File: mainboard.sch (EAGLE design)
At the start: 6 parts, among them U1 ATMEGA2560AU, U2 ITG-3200

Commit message: Added documentation
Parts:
- added IC1: FT232RLSSOP, SparkFun:FT232RLSSOP
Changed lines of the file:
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@@
 <part name="U2" library="SparkFun-Sensors" deviceset="ITG-3200" device=""/>
 <part name="U$2" library="SparkFun-Sensors" deviceset="HMC5883L" device="SMD"/>
+<part name="IC1" library="SparkFun" deviceset="FT232RL" device="SSOP"/>
 </parts>
 <sheets>
@@
 <instance part="U2" gate="G$1" x="-66.04" y="-12.7"/>
 <instance part="U$2" gate="G$1" x="-58.42" y="-60.96"/>
+<instance part="IC1" gate="G$1" x="-99.06" y="35.56"/>
 </instances>
 <busses>

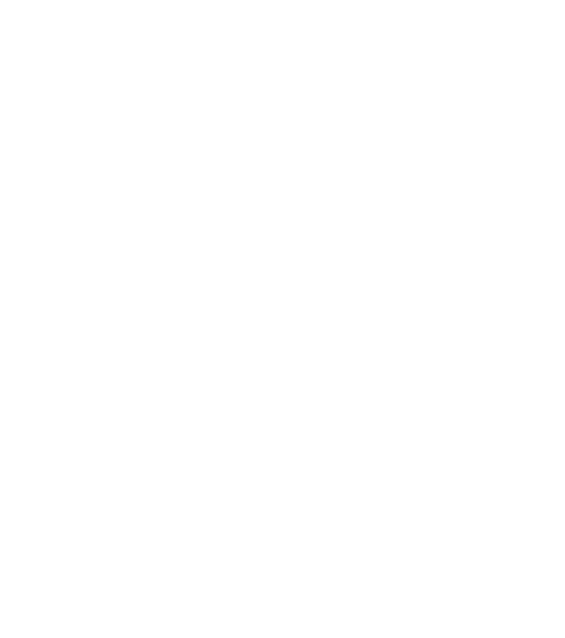
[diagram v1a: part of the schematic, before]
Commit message: Added level shifter
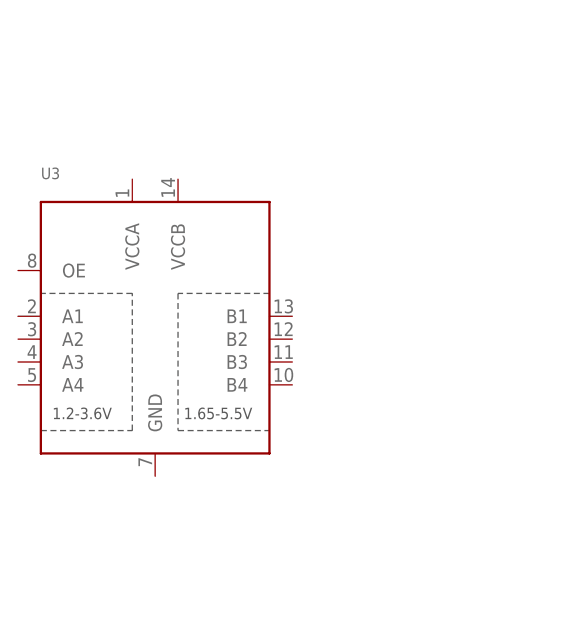
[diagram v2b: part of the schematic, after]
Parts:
- added U3: (no value), SparkFun-DigitalIC:TXB0104PWR
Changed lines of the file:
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@@
 <part name="U$2" library="SparkFun-Sensors" deviceset="HMC5883L" device="SMD"/>
 <part name="IC1" library="SparkFun" deviceset="FT232RL" device="SSOP"/>
+<part name="U3" library="SparkFun-DigitalIC" deviceset="TXB0104PWR" device=""/>
 </parts>
 <sheets>
@@
 <instance part="U$2" gate="G$1" x="-58.42" y="-60.96"/>
 <instance part="IC1" gate="G$1" x="-99.06" y="35.56"/>
+<instance part="U3" gate="G$1" x="-147.32" y="-30.48"/>
 </instances>
 <busses>

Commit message: Initial commit of power board
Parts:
- removed IC1: FT232RLSSOP, SparkFun:FT232RLSSOP
- removed U$1: RFM23BP, RFM23BP:RFM23BP
- removed U$2: HMC5883LSMD, SparkFun-Sensors:HMC5883LSMD
- added C1, C10, C2, C3, C5, C6, C7, C8, C9: 0.1uF, SparkFun:CAP0603-CAP
- added C4: 0.1uF, SparkFun:CAP0402-CAP
- added JP1, JP2: USB-SMD-NS, SparkFun-Connectors:USB-SMD-NS
- added LED2: yellow, SparkFun:LED0603
- added R1, R4, R5: 10k, SparkFun:RESISTOR0603-RES
- added R3: 10k, SparkFun:RESISTOR0402-RES
- added R7: 470, SparkFun:RESISTOR0402-RES
- added SMA1: BU-SMA-V, con-coax:BU-SMA-V
- added U4: HMC5883LSMD, SparkFun-Sensors:HMC5883LSMD
- added U5: ITG-3200, SparkFun-Sensors:ITG-3200
- added U6: (no value), SparkFun-DigitalIC:TXB0104PWR
- added U7: ATMEGA328P, SparkFun:ATMEGA168
- added U8: FT232RLSSOP, SparkFun:FT232RLSSOP
- added Y1: RESONATORSMD, SparkFun:RESONATORSMD
- added Y2: 16MHZ, SparkFun-FreqCtrl:RESONATOR16MHZ
- U1: device SparkFun-DigitalIC:ATMEGA2560AU -> SparkFun:ATMEGA2560AU
- U2: value ITG-3200 -> FT232RLSSOP; device SparkFun-Sensors:ITG-3200 -> SparkFun:FT232RLSSOP
- U3: value (none) -> RFM23BP; device SparkFun-DigitalIC:TXB0104PWR -> RFM23BP:RFM23BP
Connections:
- new net 3.3V: C6.1, C7.1, C8.1, R3.2, R4.2, R5.2, U1.AVCC, U1.VCC, U1.VCC1, U1.VCC2, U1.VCC3, U6.VCCA
- new net 5V: C2.1, C3.1, C9.1, R1.2, U3.VCC, U6.VCCB, U7.AVCC, U7.VCC@1, U7.VCC@2
- new net A0: U1.(ADC0)PF0
- new net A1: U1.(ADC1)PF1
- new net A10: U1.PK2(ADC10/PCINT18)
- new net A11: U1.PK3(ADC11/PCINT19)
- new net A12: U1.PK4(ADC12/PCINT20)
- new net A13: U1.PK5(ADC13/PCINT21)
- new net A14: U1.PK6(ADC14/PCINT22)
- new net A15: U1.PK7(ADC15/PCINT23)
- new net A2: U1.(ADC2)PF2
- new net A3: U1.(ADC3)PF3
- new net A4: U1.(ADC4/TCK)PF4
- new net A5: U1.(ADC5/TMS)PF5
- new net A6: U1.(ADC6/TDO)PF6
- new net A7: U1.(ADC7/TDI)PF7
- new net A8: U1.PK0(ADC8/PCINT16)
- new net A9: U1.PK1(ADC9/PCINT17)
- new net AREF: C5.1, U1.AREF
- new net DTR: C4.1
- new net DTR2: C1.1
- new net GND: C10.2, C2.2, C3.2, C5.2, C6.2, C7.2, C8.2, C9.2, LED2.C, SMA1.2, U1.AGND, U1.GND, U1.GND1, U1.GND2, U1.GND3, U3.GND1, U3.GND2, U3.GND3, U6.GND, U7.AGND, U7.GND@1, U7.GND@2, Y1.2, Y2.2
- new net MISO2: U3.SDO, U7.PB4(MISO)
- new net MOSI2: U3.SDI, U7.PB3(MOSI/OC2)
- new net N$1: SMA1.1, U3.ANT
- new net N$2: U7.PB6(XTAL1/TOSC1), Y2.1
- new net N$3: LED2.A, R7.1
- new net N$4: C10.1, U7.AREF
- new net N$5: U7.PB7(XTAL2/TOSC2), Y2.3
- new net N$73: U1.XTAL2, Y1.1
- new net N$74: U1.XTAL1, Y1.3
- new net PA0: U1.(AD0)PA0
- new net PA1: U1.(AD1)PA1
- new net PA2: U1.(AD2)PA2
- new net PA3: U1.(AD3)PA3
- new net PA4: U1.(AD4)PA4
- new net PA5: U1.(AD5)PA5
- new net PA6: U1.(AD6)PA6
- new net PA7: U1.(AD7)PA7
- new net PB0: U1.(SS/PCINT0)PB0
- new net PB1: U1.(SCK/PCINT1)PB1
- new net PB2: U1.(MOSI/PCINT2)PB2
- new net PB3: U1.(MISO/PCINT3)PB3
- new net PB4: U1.(OC2A/PCINT4)PB4
- new net PB5: U1.(OC1A/PCINT5)PB5
- new net PB6: U1.(OC1B/PCINT6)PB6
- new net PB7: R7.2, U1.(OC0A/OC1C/PCINT7)PB7
- new net PC0: U1.(A8)PC0
- new net PC1: U1.(A9)PC1
- new net PC2: U1.(A10)PC2
- new net PC3: U1.(A11)PC3
- new net PC4: U1.(A12)PC4
- new net PC5: U1.(A13)PC5
- new net PC6: U1.(A14)PC6
- new net PC7: U1.(A15)PC7
- new net PD7: U1.(T0)PD7
- new net PE3: U1.(OC3A/AIN1)PE3
- new net PE4: U1.(OC3B/INT4)PE4
- new net PE5: U1.(OC3C/INT5)PE5
- new net PG0: U1.(WR)PG0
- new net PG1: U1.(RD)PG1
- new net PG2: U1.(ALE)PG2
- new net PG5: U1.(OC0B)PG5
- new net PH3: U1.PH3(OC4A)
- new net PH4: U1.PH4(OC4B)
- new net PH5: U1.PH5(OC4C)
- new net PH6: U1.PH6(OC2B)
- new net PL0: U1.PL0(ICP4)
- new net PL1: U1.PL1(ICP5)
- new net PL2: U1.PL2(T5)
- new net PL3: U1.PL3(OC5A)
- new net PL4: U1.PL4(OC5B)
- new net PL5: U1.PL5(OC5C)
- new net PL6: U1.PL6
- new net PL7: U1.PL7
- new net RESET: C4.2, R3.1, U1.RESET
- new net RESET2: C1.2, R1.1, U7.PC6(/RESET)
- new net RX0: U1.(RXD0/PCIN8)PE0
- new net RX1: U1.(RXD1/INT2)PD2
- new net RX2: U1.PH0(RXD2)
- new net RX3: U1.PJ0(RXD3/PCINT9)
- new net SCK2: U3.SCK, U7.PB5(SCK)
- new net SCL: R5.1, U1.(SCL/INT0)PD0
- new net SDA: R4.1, U1.(SDA/INT1)PD1
- new net TX0: U1.(TXD0)PE1
- new net TX1: U1.(TXD1/INT3)PD3
- new net TX2: U1.PH1(TXD2)
- new net TX3: U1.PJ1(TXD3/PCINT10)
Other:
- note added: "8MHz"
- note added: "ATMEGA2560V"
- moved on the sheet: U1

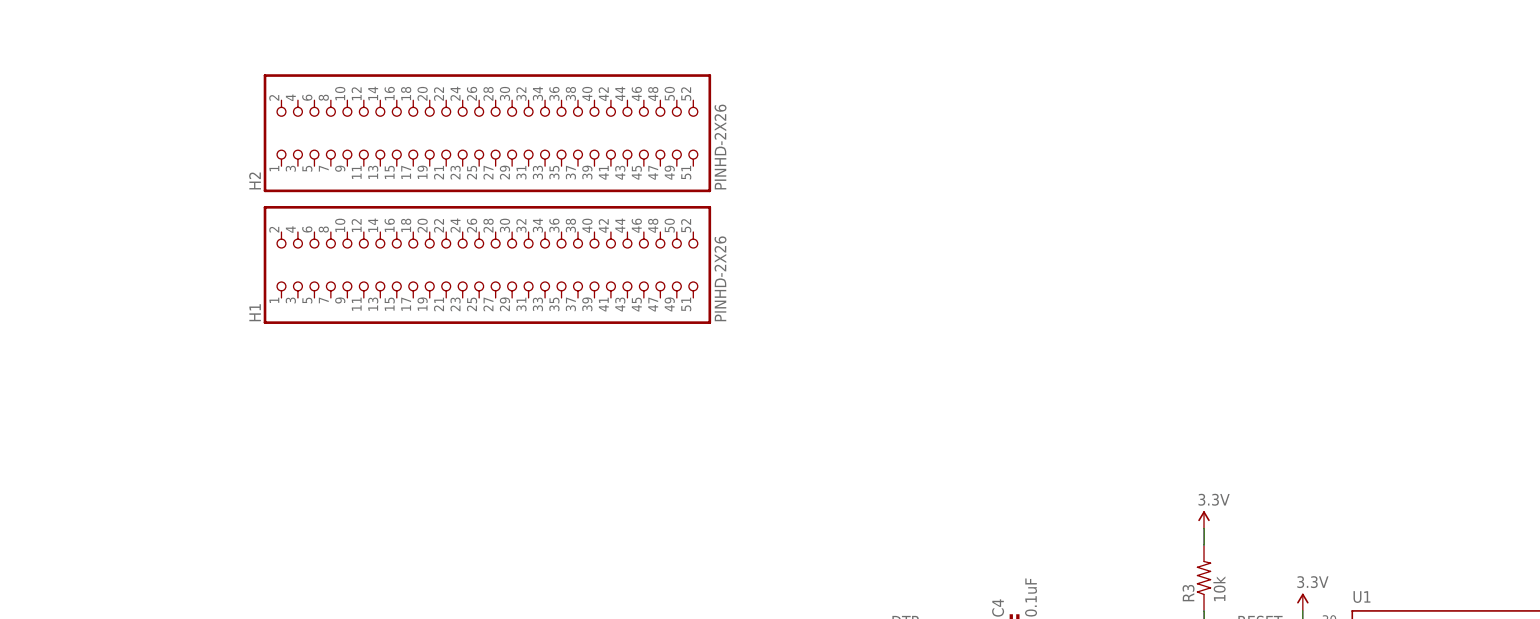
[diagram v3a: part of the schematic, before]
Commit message: Added RTC
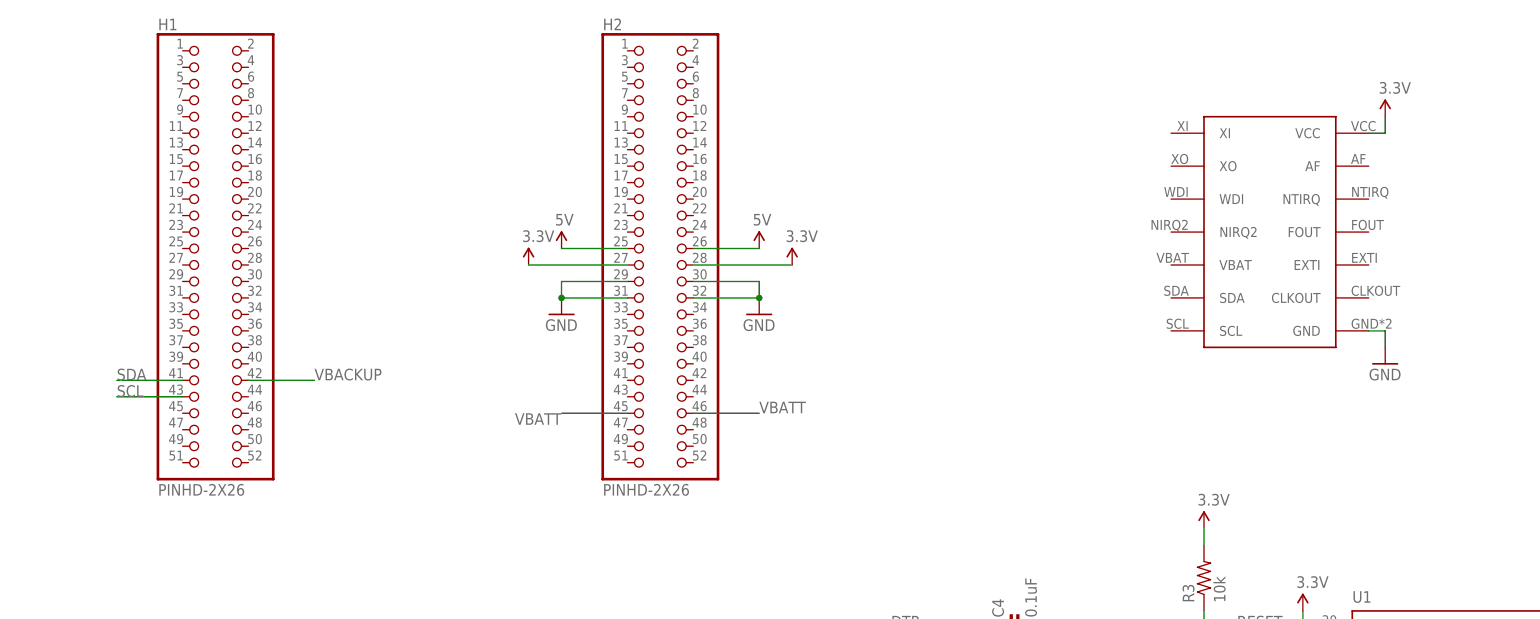
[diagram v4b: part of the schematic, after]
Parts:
- added U$1: AB0805, AB0805:AB0805
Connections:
- new net VBACKUP: H1.42
- new net VBATT: H2.45, H2.46
- net 3.3V: now also H2.27, H2.28, U$1.VCC
- net 5V: now also H2.25, H2.26
- net GND: now also H2.29, H2.30, H2.31, H2.32, U$1.GND
- net SCL: now also H1.43
- net SDA: now also H1.41
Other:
- moved on the sheet: H1, H2
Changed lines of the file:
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@@
 <part name="P+2" library="SparkFun" deviceset="3.3V" device=""/>
 <part name="GND11" library="SparkFun" deviceset="GND" device=""/>
+<part name="SUPPLY5" library="SparkFun-Aesthetics" deviceset="5V" device=""/>
+<part name="SUPPLY6" library="SparkFun-Aesthetics" deviceset="5V" device=""/>
+<part name="P+3" library="SparkFun" deviceset="3.3V" device=""/>
+<part name="P+4" library="SparkFun" deviceset="3.3V" device=""/>
+<part name="GND12" library="SparkFun" deviceset="GND" device=""/>
+<part name="GND14" library="SparkFun" deviceset="GND" device=""/>
+<part name="U$1" library="AB0805" deviceset="AB0805" device=""/>
+<part name="GND15" library="SparkFun" deviceset="GND" device=""/>
+<part name="P+7" library="SparkFun" deviceset="3.3V" device=""/>
 </parts>
 <sheets>
@@
 </plain>
 <instances>
-<instance part="H1" gate="G$1" x="50.8" y="114.3" rot="R90"/>
-<instance part="H2" gate="G$1" x="50.8" y="134.62" rot="R90"/>
+<instance part="H1" gate="G$1" x="10.16" y="116.84"/>
+<instance part="H2" gate="G$1" x="78.74" y="116.84"/>
 <instance part="U3" gate="G$1" x="-45.72" y="50.8"/>
 <instance part="U5" gate="G$1" x="347.98" y="0"/>
@@
 <instance part="P+2" gate="G$1" x="50.8" y="12.7"/>
 <instance part="GND11" gate="1" x="53.34" y="-27.94"/>
+<instance part="SUPPLY5" gate="G$1" x="63.5" y="116.84"/>
+<instance part="SUPPLY6" gate="G$1" x="93.98" y="116.84"/>
+<instance part="P+3" gate="G$1" x="58.42" y="114.3"/>
+<instance part="P+4" gate="G$1" x="99.06" y="114.3"/>
+<instance part="GND12" gate="1" x="63.5" y="106.68"/>
+<instance part="GND14" gate="1" x="93.98" y="106.68"/>
+<instance part="U$1" gate="G$1" x="172.72" y="119.38"/>
+<instance part="GND15" gate="1" x="190.5" y="99.06"/>
+<instance part="P+7" gate="G$1" x="190.5" y="137.16"/>
 </instances>
 <busses>
@@
 <wire x1="53.34" y1="-25.4" x2="53.34" y2="-22.86" width="0.1524" layer="91"/>
 </segment>
+<segment>
+<pinref part="H2" gate="G$1" pin="29"/>
+<wire x1="73.66" y1="111.76" x2="63.5" y2="111.76" width="0.1524" layer="91"/>
+<pinref part="H2" gate="G$1" pin="31"/>
+<wire x1="73.66" y1="109.22" x2="63.5" y2="109.22" width="0.1524" layer="91"/>
+<wire x1="63.5" y1="111.76" x2="63.5" y2="109.22" width="0.1524" layer="91"/>
+<pinref part="GND12" gate="1" pin="GND"/>
+<junction x="63.5" y="109.22"/>
+</segment>
+<segment>
+<pinref part="H2" gate="G$1" pin="30"/>
+<wire x1="83.82" y1="111.76" x2="93.98" y2="111.76" width="0.1524" layer="91"/>
+<pinref part="H2" gate="G$1" pin="32"/>
+<wire x1="83.82" y1="109.22" x2="93.98" y2="109.22" width="0.1524" layer="91"/>
+<wire x1="93.98" y1="111.76" x2="93.98" y2="109.22" width="0.1524" layer="91"/>
+<pinref part="GND14" gate="1" pin="GND"/>
+<junction x="93.98" y="109.22"/>
+</segment>
+<segment>
+<pinref part="U$1" gate="G$1" pin="GND"/>
+<wire x1="187.96" y1="104.14" x2="190.5" y2="104.14" width="0.1524" layer="91"/>
+<wire x1="190.5" y1="104.14" x2="190.5" y2="101.6" width="0.1524" layer="91"/>
+<pinref part="GND15" gate="1" pin="GND"/>
+</segment>
 </net>
 <net name="N$73" class="0">
@@
 <pinref part="R5" gate="G$1" pin="1"/>
 </segment>
+<segment>
+<pinref part="H1" gate="G$1" pin="43"/>
+<wire x1="5.08" y1="93.98" x2="-5.08" y2="93.98" width="0.1524" layer="91"/>
+<label x="-5.08" y="93.98" size="1.778" layer="95"/>
+</segment>
 </net>
 <net name="SDA" class="0">
@@
 <pinref part="R4" gate="G$1" pin="1"/>
 <pinref part="U1" gate="1" pin="(SDA/INT1)PD1"/>
+</segment>
+<segment>
+<pinref part="H1" gate="G$1" pin="41"/>
+<wire x1="5.08" y1="96.52" x2="-5.08" y2="96.52" width="0.1524" layer="91"/>
+<label x="-5.08" y="96.52" size="1.778" layer="95"/>
 </segment>
 </net>
@@
 <wire x1="50.8" y1="12.7" x2="50.8" y2="10.16" width="0.1524" layer="91"/>
 </segment>
+<segment>
+<pinref part="H2" gate="G$1" pin="27"/>
+<wire x1="73.66" y1="114.3" x2="58.42" y2="114.3" width="0.1524" layer="91"/>
+<pinref part="P+3" gate="G$1" pin="3.3V"/>
+</segment>
+<segment>
+<pinref part="H2" gate="G$1" pin="28"/>
+<wire x1="83.82" y1="114.3" x2="99.06" y2="114.3" width="0.1524" layer="91"/>
+<pinref part="P+4" gate="G$1" pin="3.3V"/>
+</segment>
+<segment>
+<pinref part="U$1" gate="G$1" pin="VCC"/>
+<pinref part="P+7" gate="G$1" pin="3.3V"/>
+<wire x1="187.96" y1="134.62" x2="190.5" y2="134.62" width="0.1524" layer="91"/>
+<wire x1="190.5" y1="134.62" x2="190.5" y2="137.16" width="0.1524" layer="91"/>
+</segment>
 </net>
 <net name="RESET2" class="0">
@@
 </segment>
 <segment>
+<pinref part="SUPPLY2" gate="G$1" pin="5V"/>
 <pinref part="U3" gate="G$1" pin="VCC"/>
-<pinref part="SUPPLY2" gate="G$1" pin="5V"/>
 <wire x1="-45.72" y1="66.04" x2="-45.72" y2="68.58" width="0.1524" layer="91"/>
 </segment>
@@
 <wire x1="55.88" y1="10.16" x2="55.88" y2="12.7" width="0.1524" layer="91"/>
 </segment>
+<segment>
+<pinref part="H2" gate="G$1" pin="25"/>
+<wire x1="73.66" y1="116.84" x2="63.5" y2="116.84" width="0.1524" layer="91"/>
+<pinref part="SUPPLY5" gate="G$1" pin="5V"/>
+</segment>
+<segment>
+<pinref part="H2" gate="G$1" pin="26"/>
+<wire x1="83.82" y1="116.84" x2="93.98" y2="116.84" width="0.1524" layer="91"/>
+<pinref part="SUPPLY6" gate="G$1" pin="5V"/>
+</segment>
 </net>
 <net name="N$1" class="0">
@@
 </segment>
 </net>
+<net name="VBATT" class="0">
+<segment>
+<pinref part="H2" gate="G$1" pin="45"/>
+<wire x1="73.66" y1="91.44" x2="63.5" y2="91.44" width="0.1524" layer="91"/>
+<label x="63.5" y="91.44" size="1.778" layer="95" rot="R180"/>
+</segment>
+<segment>
+<pinref part="H2" gate="G$1" pin="46"/>
+<wire x1="83.82" y1="91.44" x2="93.98" y2="91.44" width="0.1524" layer="91"/>
+<label x="93.98" y="91.44" size="1.778" layer="95"/>
+</segment>
+</net>
+<net name="VBACKUP" class="0">
+<segment>
+<pinref part="H1" gate="G$1" pin="42"/>
+<wire x1="15.24" y1="96.52" x2="25.4" y2="96.52" width="0.1524" layer="91"/>
+<label x="25.4" y="96.52" size="1.778" layer="95"/>
+</segment>
+</net>

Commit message: Added Micrel voltage supervisors
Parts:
- added U10: MIC803-46D3VM3TR, Micrel:MIC803-46D3VM3TR
- added U9: MIC803-31D3VM3TR, Micrel:MIC803-31D3VM3TR
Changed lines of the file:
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@@
 <part name="GND15" library="SparkFun" deviceset="GND" device=""/>
 <part name="P+7" library="SparkFun" deviceset="3.3V" device=""/>
+<part name="U9" library="Micrel" deviceset="MIC803-31D3VM3TR" device=""/>
+<part name="U10" library="Micrel" deviceset="MIC803-46D3VM3TR" device=""/>
 </parts>
 <sheets>
@@
 <instance part="GND13" gate="1" x="271.78" y="5.08"/>
 <instance part="P+1" gate="G$1" x="162.56" y="73.66"/>
-<instance part="P+5" gate="G$1" x="177.8" y="60.96"/>
+<instance part="P+5" gate="G$1" x="177.8" y="83.82"/>
 <instance part="P+6" gate="G$1" x="271.78" y="-7.62"/>
 <instance part="U7" gate="G$1" x="-114.3" y="-22.86" smashed="yes">
@@
 <instance part="GND12" gate="1" x="63.5" y="106.68"/>
 <instance part="GND14" gate="1" x="93.98" y="106.68"/>
-<instance part="U$1" gate="G$1" x="172.72" y="119.38"/>
-<instance part="GND15" gate="1" x="190.5" y="99.06"/>
-<instance part="P+7" gate="G$1" x="190.5" y="137.16"/>
+<instance part="U$1" gate="G$1" x="317.5" y="88.9"/>
+<instance part="GND15" gate="1" x="335.28" y="68.58"/>
+<instance part="P+7" gate="G$1" x="335.28" y="106.68"/>
+<instance part="U9" gate="A" x="180.34" y="109.22"/>
+<instance part="U10" gate="A" x="-139.7" y="30.48"/>
 </instances>
 <busses>
@@
 <segment>
 <pinref part="U$1" gate="G$1" pin="GND"/>
-<wire x1="187.96" y1="104.14" x2="190.5" y2="104.14" width="0.1524" layer="91"/>
-<wire x1="190.5" y1="104.14" x2="190.5" y2="101.6" width="0.1524" layer="91"/>
+<wire x1="332.74" y1="73.66" x2="335.28" y2="73.66" width="0.1524" layer="91"/>
+<wire x1="335.28" y1="73.66" x2="335.28" y2="71.12" width="0.1524" layer="91"/>
 <pinref part="GND15" gate="1" pin="GND"/>
 </segment>
@@
 <segment>
 <wire x1="180.34" y1="40.64" x2="177.8" y2="40.64" width="0.1524" layer="91"/>
-<wire x1="177.8" y1="40.64" x2="177.8" y2="60.96" width="0.1524" layer="91"/>
+<wire x1="177.8" y1="40.64" x2="177.8" y2="83.82" width="0.1524" layer="91"/>
 <wire x1="180.34" y1="30.48" x2="177.8" y2="30.48" width="0.1524" layer="91"/>
 <wire x1="177.8" y1="30.48" x2="177.8" y2="40.64" width="0.1524" layer="91"/>
@@
 <pinref part="U$1" gate="G$1" pin="VCC"/>
 <pinref part="P+7" gate="G$1" pin="3.3V"/>
-<wire x1="187.96" y1="134.62" x2="190.5" y2="134.62" width="0.1524" layer="91"/>
-<wire x1="190.5" y1="134.62" x2="190.5" y2="137.16" width="0.1524" layer="91"/>
-</segment>
-</net>
+<wire x1="332.74" y1="104.14" x2="335.28" y2="104.14" width="0.1524" layer="91"/>
+<wire x1="335.28" y1="104.14" x2="335.28" y2="106.68" width="0.1524" layer="91"/>
+</segment>
+</net>
